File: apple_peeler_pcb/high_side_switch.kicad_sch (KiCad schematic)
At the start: 7 parts, among them Q13 2N7002, Q14 AO3401A

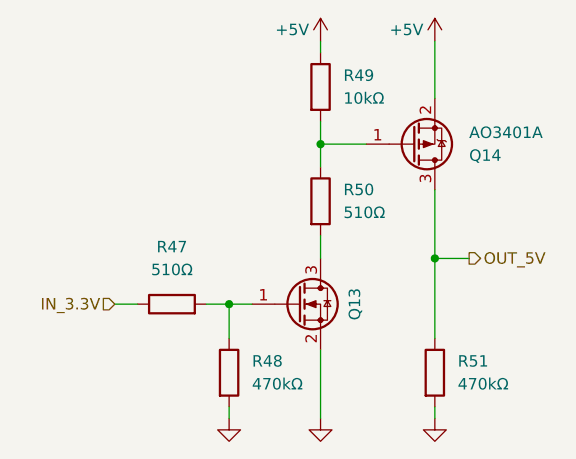
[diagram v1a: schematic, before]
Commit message: replace fancy debug connectors by pin header to save $8
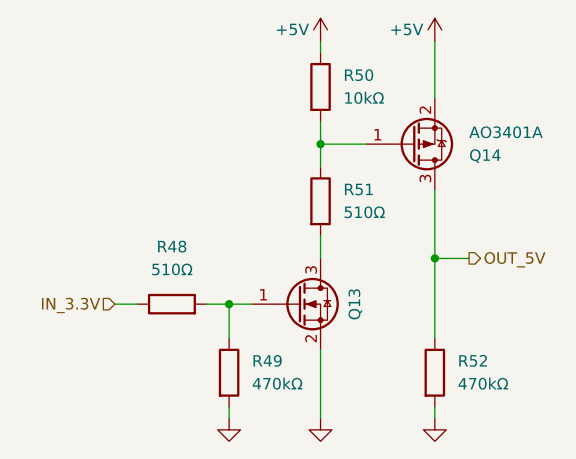
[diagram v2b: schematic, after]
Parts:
- renumbered R47 to R48, R48 to R49, R49 to R50, R50 to R51, R51 to R52
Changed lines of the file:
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@@
 		(on_board yes)
 		(dnp no)
-		(property "Reference" "#PWR0118"
+		(property "Reference" "#PWR0116"
 			(at 153.67 128.27 0)
 			(effects
@@
 			(project "apple_peeler_pcb"
 				(path "/d5946b96-44a8-4a28-8641-19803e1510af/ab4760da-4146-4688-a275-418314974b55/207d6e2c-5657-4cae-9098-bf31bbf0eeb3/3e7a2019-c147-43be-8925-3656ede786af"
-					(reference "#PWR0123")
-					(unit 1)
-				)
-				(path "/d5946b96-44a8-4a28-8641-19803e1510af/ab4760da-4146-4688-a275-418314974b55/216077bc-1e97-451f-9a4f-0a4e0691e85e/3e7a2019-c147-43be-8925-3656ede786af"
-					(reference "#PWR0118")
+					(reference "#PWR0121")
+					(unit 1)
+				)
+				(path "/d5946b96-44a8-4a28-8641-19803e1510af/ab4760da-4146-4688-a275-418314974b55/216077bc-1e97-451f-9a4f-0a4e0691e85e/3e7a2019-c147-43be-8925-3656ede786af"
+					(reference "#PWR0116")
 					(unit 1)
 				)
@@
 		(on_board yes)
 		(dnp no)
-		(property "Reference" "#PWR0117"
+		(property "Reference" "#PWR0115"
 			(at 153.67 83.82 0)
 			(effects
@@
 			(project "apple_peeler_pcb"
 				(path "/d5946b96-44a8-4a28-8641-19803e1510af/ab4760da-4146-4688-a275-418314974b55/207d6e2c-5657-4cae-9098-bf31bbf0eeb3/3e7a2019-c147-43be-8925-3656ede786af"
-					(reference "#PWR0122")
-					(unit 1)
-				)
-				(path "/d5946b96-44a8-4a28-8641-19803e1510af/ab4760da-4146-4688-a275-418314974b55/216077bc-1e97-451f-9a4f-0a4e0691e85e/3e7a2019-c147-43be-8925-3656ede786af"
-					(reference "#PWR0117")
+					(reference "#PWR0120")
+					(unit 1)
+				)
+				(path "/d5946b96-44a8-4a28-8641-19803e1510af/ab4760da-4146-4688-a275-418314974b55/216077bc-1e97-451f-9a4f-0a4e0691e85e/3e7a2019-c147-43be-8925-3656ede786af"
+					(reference "#PWR0115")
 					(unit 1)
 				)
@@
 		(dnp no)
 		(fields_autoplaced yes)
-		(property "Reference" "R49"
+		(property "Reference" "R50"
 			(at 143.51 83.8199 0)
 			(effects
@@
 			(project "apple_peeler_pcb"
 				(path "/d5946b96-44a8-4a28-8641-19803e1510af/ab4760da-4146-4688-a275-418314974b55/207d6e2c-5657-4cae-9098-bf31bbf0eeb3/3e7a2019-c147-43be-8925-3656ede786af"
-					(reference "R54")
-					(unit 1)
-				)
-				(path "/d5946b96-44a8-4a28-8641-19803e1510af/ab4760da-4146-4688-a275-418314974b55/216077bc-1e97-451f-9a4f-0a4e0691e85e/3e7a2019-c147-43be-8925-3656ede786af"
-					(reference "R49")
+					(reference "R55")
+					(unit 1)
+				)
+				(path "/d5946b96-44a8-4a28-8641-19803e1510af/ab4760da-4146-4688-a275-418314974b55/216077bc-1e97-451f-9a4f-0a4e0691e85e/3e7a2019-c147-43be-8925-3656ede786af"
+					(reference "R50")
 					(unit 1)
 				)
@@
 		(on_board yes)
 		(dnp no)
-		(property "Reference" "#PWR0115"
+		(property "Reference" "#PWR0113"
 			(at 140.97 83.82 0)
 			(effects
@@
 			(project "apple_peeler_pcb"
 				(path "/d5946b96-44a8-4a28-8641-19803e1510af/ab4760da-4146-4688-a275-418314974b55/207d6e2c-5657-4cae-9098-bf31bbf0eeb3/3e7a2019-c147-43be-8925-3656ede786af"
-					(reference "#PWR0120")
-					(unit 1)
-				)
-				(path "/d5946b96-44a8-4a28-8641-19803e1510af/ab4760da-4146-4688-a275-418314974b55/216077bc-1e97-451f-9a4f-0a4e0691e85e/3e7a2019-c147-43be-8925-3656ede786af"
-					(reference "#PWR0115")
+					(reference "#PWR0118")
+					(unit 1)
+				)
+				(path "/d5946b96-44a8-4a28-8641-19803e1510af/ab4760da-4146-4688-a275-418314974b55/216077bc-1e97-451f-9a4f-0a4e0691e85e/3e7a2019-c147-43be-8925-3656ede786af"
+					(reference "#PWR0113")
 					(unit 1)
 				)
@@
 		(dnp no)
 		(fields_autoplaced yes)
-		(property "Reference" "R50"
+		(property "Reference" "R51"
 			(at 143.51 96.5199 0)
 			(effects
@@
 			(project "apple_peeler_pcb"
 				(path "/d5946b96-44a8-4a28-8641-19803e1510af/ab4760da-4146-4688-a275-418314974b55/207d6e2c-5657-4cae-9098-bf31bbf0eeb3/3e7a2019-c147-43be-8925-3656ede786af"
-					(reference "R55")
-					(unit 1)
-				)
-				(path "/d5946b96-44a8-4a28-8641-19803e1510af/ab4760da-4146-4688-a275-418314974b55/216077bc-1e97-451f-9a4f-0a4e0691e85e/3e7a2019-c147-43be-8925-3656ede786af"
-					(reference "R50")
+					(reference "R56")
+					(unit 1)
+				)
+				(path "/d5946b96-44a8-4a28-8641-19803e1510af/ab4760da-4146-4688-a275-418314974b55/216077bc-1e97-451f-9a4f-0a4e0691e85e/3e7a2019-c147-43be-8925-3656ede786af"
+					(reference "R51")
 					(unit 1)
 				)
@@
 		(dnp no)
 		(fields_autoplaced yes)
-		(property "Reference" "R47"
+		(property "Reference" "R48"
 			(at 124.46 102.87 90)
 			(effects
@@
 			(project "apple_peeler_pcb"
 				(path "/d5946b96-44a8-4a28-8641-19803e1510af/ab4760da-4146-4688-a275-418314974b55/207d6e2c-5657-4cae-9098-bf31bbf0eeb3/3e7a2019-c147-43be-8925-3656ede786af"
-					(reference "R52")
-					(unit 1)
-				)
-				(path "/d5946b96-44a8-4a28-8641-19803e1510af/ab4760da-4146-4688-a275-418314974b55/216077bc-1e97-451f-9a4f-0a4e0691e85e/3e7a2019-c147-43be-8925-3656ede786af"
-					(reference "R47")
+					(reference "R53")
+					(unit 1)
+				)
+				(path "/d5946b96-44a8-4a28-8641-19803e1510af/ab4760da-4146-4688-a275-418314974b55/216077bc-1e97-451f-9a4f-0a4e0691e85e/3e7a2019-c147-43be-8925-3656ede786af"
+					(reference "R48")
 					(unit 1)
 				)
@@
 		(on_board yes)
 		(dnp no)
-		(property "Reference" "#PWR0116"
+		(property "Reference" "#PWR0114"
 			(at 140.97 128.27 0)
 			(effects
@@
 			(project "apple_peeler_pcb"
 				(path "/d5946b96-44a8-4a28-8641-19803e1510af/ab4760da-4146-4688-a275-418314974b55/207d6e2c-5657-4cae-9098-bf31bbf0eeb3/3e7a2019-c147-43be-8925-3656ede786af"
-					(reference "#PWR0121")
-					(unit 1)
-				)
-				(path "/d5946b96-44a8-4a28-8641-19803e1510af/ab4760da-4146-4688-a275-418314974b55/216077bc-1e97-451f-9a4f-0a4e0691e85e/3e7a2019-c147-43be-8925-3656ede786af"
-					(reference "#PWR0116")
+					(reference "#PWR0119")
+					(unit 1)
+				)
+				(path "/d5946b96-44a8-4a28-8641-19803e1510af/ab4760da-4146-4688-a275-418314974b55/216077bc-1e97-451f-9a4f-0a4e0691e85e/3e7a2019-c147-43be-8925-3656ede786af"
+					(reference "#PWR0114")
 					(unit 1)
 				)
@@
 		(on_board yes)
 		(dnp no)
-		(property "Reference" "#PWR0114"
+		(property "Reference" "#PWR0112"
 			(at 130.81 128.27 0)
 			(effects
@@
 			(project "apple_peeler_pcb"
 				(path "/d5946b96-44a8-4a28-8641-19803e1510af/ab4760da-4146-4688-a275-418314974b55/207d6e2c-5657-4cae-9098-bf31bbf0eeb3/3e7a2019-c147-43be-8925-3656ede786af"
-					(reference "#PWR0119")
-					(unit 1)
-				)
-				(path "/d5946b96-44a8-4a28-8641-19803e1510af/ab4760da-4146-4688-a275-418314974b55/216077bc-1e97-451f-9a4f-0a4e0691e85e/3e7a2019-c147-43be-8925-3656ede786af"
-					(reference "#PWR0114")
+					(reference "#PWR0117")
+					(unit 1)
+				)
+				(path "/d5946b96-44a8-4a28-8641-19803e1510af/ab4760da-4146-4688-a275-418314974b55/216077bc-1e97-451f-9a4f-0a4e0691e85e/3e7a2019-c147-43be-8925-3656ede786af"
+					(reference "#PWR0112")
 					(unit 1)
 				)
@@
 		(dnp no)
 		(fields_autoplaced yes)
-		(property "Reference" "R51"
+		(property "Reference" "R52"
 			(at 156.21 115.5699 0)
 			(effects
@@
 			(project "apple_peeler_pcb"
 				(path "/d5946b96-44a8-4a28-8641-19803e1510af/ab4760da-4146-4688-a275-418314974b55/207d6e2c-5657-4cae-9098-bf31bbf0eeb3/3e7a2019-c147-43be-8925-3656ede786af"
-					(reference "R56")
-					(unit 1)
-				)
-				(path "/d5946b96-44a8-4a28-8641-19803e1510af/ab4760da-4146-4688-a275-418314974b55/216077bc-1e97-451f-9a4f-0a4e0691e85e/3e7a2019-c147-43be-8925-3656ede786af"
-					(reference "R51")
+					(reference "R57")
+					(unit 1)
+				)
+				(path "/d5946b96-44a8-4a28-8641-19803e1510af/ab4760da-4146-4688-a275-418314974b55/216077bc-1e97-451f-9a4f-0a4e0691e85e/3e7a2019-c147-43be-8925-3656ede786af"
+					(reference "R52")
 					(unit 1)
 				)
@@
 		(dnp no)
 		(fields_autoplaced yes)
-		(property "Reference" "R48"
+		(property "Reference" "R49"
 			(at 133.35 115.5699 0)
 			(effects
@@
 			(project "apple_peeler_pcb"
 				(path "/d5946b96-44a8-4a28-8641-19803e1510af/ab4760da-4146-4688-a275-418314974b55/207d6e2c-5657-4cae-9098-bf31bbf0eeb3/3e7a2019-c147-43be-8925-3656ede786af"
-					(reference "R53")
-					(unit 1)
-				)
-				(path "/d5946b96-44a8-4a28-8641-19803e1510af/ab4760da-4146-4688-a275-418314974b55/216077bc-1e97-451f-9a4f-0a4e0691e85e/3e7a2019-c147-43be-8925-3656ede786af"
-					(reference "R48")
-					(unit 1)
-				)
+					(reference "R54")
+					(unit 1)
+				)
+				(path "/d5946b96-44a8-4a28-8641-19803e1510af/ab4760da-4146-4688-a275-418314974b55/216077bc-1e97-451f-9a4f-0a4e0691e85e/3e7a2019-c147-43be-8925-3656ede786af"
+					(reference "R49")
+					(unit 1)
+				)
